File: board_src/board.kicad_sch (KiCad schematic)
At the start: 14 parts, among them J1 Conn_01x05, J16 Conn_01x05, J17 Conn_01x05, J18 Conn_02x20_Counter_Clockwise, J20 Conn_02x20_Counter_Clockwise, J21 Conn_02x20_Counter_Clockwise, J22 Conn_02x20_Counter_Clockwise, J6 Conn_01x03, J7 Conn_01x02, J8 Conn_01x03, SW1 SW_Push, SW2 SW_Push, U1 Pico, U4 Pico

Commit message: wersja 3d
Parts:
- removed J7: Conn_01x02, Connector_PinHeader_2.54mm:PinHeader_1x02_P2.54mm_Vertical, symbol Connector_Generic:Conn_01x02
- removed SW1, SW2: SW_Push, Button_Switch_THT:SW_PUSH_6mm, symbol Switch:SW_Push
- added J7: Conn_01x16, Connector_PinSocket_2.54mm:PinSocket_1x16_P2.54mm_Vertical, symbol Connector:Conn_01x16_Socket
- added S1, S2: 1301.9319, footprints:przycisk, symbol przycisk:1301.9319
- J18, J20, J21, J22: symbol Connector_Generic:Conn_02x20_Counter_Clockwise -> Connector_Generic:Conn_02x20_Odd_Even
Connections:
- net GND: now also S1.1 (NO_1), S2.1 (NO_1)
- net a1: now also J18.2 (Pin_2); no longer J18.40 (Pin_40)
- net a10: now also J18.19 (Pin_19), J18.20 (Pin_20); no longer J18.10 (Pin_10), J18.31 (Pin_31)
- net a11: now also J18.21 (Pin_21), J18.22 (Pin_22); no longer J18.11 (Pin_11), J18.30 (Pin_30)
- net a12: now also J18.23 (Pin_23), J18.24 (Pin_24); no longer J18.12 (Pin_12), J18.29 (Pin_29)
- net a13: now also J18.25 (Pin_25), J18.26 (Pin_26); no longer J18.13 (Pin_13), J18.28 (Pin_28)
- net a14: now also J18.28 (Pin_28); no longer J18.14 (Pin_14)
- net a15: now also J18.29 (Pin_29), J18.30 (Pin_30); no longer J18.15 (Pin_15), J18.26 (Pin_26)
- net a16: now also J18.31 (Pin_31), J18.32 (Pin_32); no longer J18.16 (Pin_16), J18.25 (Pin_25)
- net a17: now also J18.33 (Pin_33), J18.34 (Pin_34); no longer J18.17 (Pin_17), J18.24 (Pin_24)
- net a18: now also J18.35 (Pin_35), J18.36 (Pin_36); no longer J18.18 (Pin_18), J18.23 (Pin_23)
- net a19: now also J18.37 (Pin_37), J18.38 (Pin_38); no longer J18.19 (Pin_19), J18.22 (Pin_22)
- net a2: now also J18.3 (Pin_3), J18.4 (Pin_4); no longer J18.2 (Pin_2), J18.39 (Pin_39)
- net a20: now also J18.39 (Pin_39), J18.40 (Pin_40); no longer J18.20 (Pin_20), J18.21 (Pin_21)
- net a3: now also J18.5 (Pin_5), J18.6 (Pin_6); no longer J18.3 (Pin_3), J18.38 (Pin_38)
- net a4: now also J18.7 (Pin_7), J18.8 (Pin_8); no longer J18.37 (Pin_37), J18.4 (Pin_4)
- net a5: now also J18.10 (Pin_10), J18.9 (Pin_9); no longer J18.36 (Pin_36), J18.5 (Pin_5)
- net a6: now also J18.11 (Pin_11), J18.12 (Pin_12); no longer J18.35 (Pin_35), J18.6 (Pin_6)
- net a7: now also J18.13 (Pin_13), J18.14 (Pin_14); no longer J18.34 (Pin_34), J18.7 (Pin_7)
- net a8: now also J18.15 (Pin_15), J18.16 (Pin_16); no longer J18.33 (Pin_33), J18.8 (Pin_8)
- net a9: now also J18.17 (Pin_17), J18.18 (Pin_18); no longer J18.32 (Pin_32), J18.9 (Pin_9)
- net b1: now also J20.2 (Pin_2); no longer J20.40 (Pin_40)
- net b10: now also J20.19 (Pin_19), J20.20 (Pin_20); no longer J20.10 (Pin_10), J20.31 (Pin_31)
- net b11: now also J20.21 (Pin_21), J20.22 (Pin_22), S1.3 (COM_1); no longer J20.11 (Pin_11), J20.30 (Pin_30)
- net b12: now also J20.23 (Pin_23), J20.24 (Pin_24); no longer J20.12 (Pin_12), J20.29 (Pin_29)
- net b13: now also J20.25 (Pin_25), J20.26 (Pin_26); no longer J20.13 (Pin_13), J20.28 (Pin_28)
- net b14: now also J20.28 (Pin_28); no longer J20.14 (Pin_14)
- net b15: now also J20.29 (Pin_29), J20.30 (Pin_30); no longer J20.15 (Pin_15), J20.26 (Pin_26)
- net b16: now also J20.31 (Pin_31), J20.32 (Pin_32); no longer J20.16 (Pin_16), J20.25 (Pin_25)
- net b17: now also J20.33 (Pin_33), J20.34 (Pin_34); no longer J20.17 (Pin_17), J20.24 (Pin_24)
- net b18: now also J20.35 (Pin_35), J20.36 (Pin_36); no longer J20.18 (Pin_18), J20.23 (Pin_23)
- net b19: now also J20.37 (Pin_37), J20.38 (Pin_38); no longer J20.19 (Pin_19), J20.22 (Pin_22)
- net b2: now also J20.3 (Pin_3), J20.4 (Pin_4); no longer J20.2 (Pin_2), J20.39 (Pin_39)
- net b20: now also J20.39 (Pin_39), J20.40 (Pin_40); no longer J20.20 (Pin_20), J20.21 (Pin_21)
- net b3: now also J20.5 (Pin_5), J20.6 (Pin_6); no longer J20.3 (Pin_3), J20.38 (Pin_38)
- net b4: now also J20.7 (Pin_7), J20.8 (Pin_8); no longer J20.37 (Pin_37), J20.4 (Pin_4)
- net b5: now also J20.10 (Pin_10), J20.9 (Pin_9); no longer J20.36 (Pin_36), J20.5 (Pin_5)
- net b6: now also J20.11 (Pin_11), J20.12 (Pin_12); no longer J20.35 (Pin_35), J20.6 (Pin_6)
- net b7: now also J20.13 (Pin_13), J20.14 (Pin_14); no longer J20.34 (Pin_34), J20.7 (Pin_7)
- net b8: now also J20.15 (Pin_15), J20.16 (Pin_16); no longer J20.33 (Pin_33), J20.8 (Pin_8)
- net b9: now also J20.17 (Pin_17), J20.18 (Pin_18); no longer J20.32 (Pin_32), J20.9 (Pin_9)
- net c1: now also J21.2 (Pin_2); no longer J21.40 (Pin_40)
- net c10: now also J21.19 (Pin_19), J21.20 (Pin_20); no longer J21.10 (Pin_10), J21.31 (Pin_31)
- net c11: now also J21.21 (Pin_21), J21.22 (Pin_22); no longer J21.11 (Pin_11), J21.30 (Pin_30)
- net c12: now also J21.23 (Pin_23), J21.24 (Pin_24); no longer J21.12 (Pin_12), J21.29 (Pin_29)
- net c13: now also J21.25 (Pin_25), J21.26 (Pin_26); no longer J21.13 (Pin_13), J21.28 (Pin_28)
- net c14: now also J21.28 (Pin_28); no longer J21.14 (Pin_14)
- net c15: now also J21.29 (Pin_29), J21.30 (Pin_30); no longer J21.15 (Pin_15), J21.26 (Pin_26)
- net c16: now also J21.31 (Pin_31), J21.32 (Pin_32); no longer J21.16 (Pin_16), J21.25 (Pin_25)
- net c17: now also J21.33 (Pin_33), J21.34 (Pin_34); no longer J21.17 (Pin_17), J21.24 (Pin_24)
- net c18: now also J21.35 (Pin_35), J21.36 (Pin_36); no longer J21.18 (Pin_18), J21.23 (Pin_23)
- net c19: now also J21.37 (Pin_37), J21.38 (Pin_38); no longer J21.19 (Pin_19), J21.22 (Pin_22)
- net c2: now also J21.3 (Pin_3), J21.4 (Pin_4); no longer J21.2 (Pin_2), J21.39 (Pin_39)
- net c20: now also J21.39 (Pin_39), J21.40 (Pin_40); no longer J21.20 (Pin_20), J21.21 (Pin_21)
- net c3: now also J21.5 (Pin_5), J21.6 (Pin_6); no longer J21.3 (Pin_3), J21.38 (Pin_38)
- net c4: now also J21.7 (Pin_7), J21.8 (Pin_8); no longer J21.37 (Pin_37), J21.4 (Pin_4)
- net c5: now also J21.10 (Pin_10), J21.9 (Pin_9); no longer J21.36 (Pin_36), J21.5 (Pin_5)
- net c6: now also J21.11 (Pin_11), J21.12 (Pin_12); no longer J21.35 (Pin_35), J21.6 (Pin_6)
- net c7: now also J21.13 (Pin_13), J21.14 (Pin_14); no longer J21.34 (Pin_34), J21.7 (Pin_7)
- net c8: now also J21.15 (Pin_15), J21.16 (Pin_16); no longer J21.33 (Pin_33), J21.8 (Pin_8)
- net c9: now also J21.17 (Pin_17), J21.18 (Pin_18); no longer J21.32 (Pin_32), J21.9 (Pin_9)
- net d1: now also J22.2 (Pin_2); no longer J22.40 (Pin_40)
- net d10: now also J22.19 (Pin_19), J22.20 (Pin_20); no longer J22.10 (Pin_10), J22.31 (Pin_31)
- net d11: now also J22.21 (Pin_21), J22.22 (Pin_22), S2.3 (COM_1); no longer J22.11 (Pin_11), J22.30 (Pin_30)
- net d12: now also J22.23 (Pin_23), J22.24 (Pin_24); no longer J22.12 (Pin_12), J22.29 (Pin_29)
- net d13: now also J22.25 (Pin_25), J22.26 (Pin_26); no longer J22.13 (Pin_13), J22.28 (Pin_28)
- net d14: now also J22.28 (Pin_28); no longer J22.14 (Pin_14)
- net d15: now also J22.29 (Pin_29), J22.30 (Pin_30); no longer J22.15 (Pin_15), J22.26 (Pin_26)
- net d16: now also J22.31 (Pin_31), J22.32 (Pin_32); no longer J22.16 (Pin_16), J22.25 (Pin_25)
- net d17: now also J22.33 (Pin_33), J22.34 (Pin_34); no longer J22.17 (Pin_17), J22.24 (Pin_24)
- net d18: now also J22.35 (Pin_35), J22.36 (Pin_36); no longer J22.18 (Pin_18), J22.23 (Pin_23)
- net d19: now also J22.37 (Pin_37), J22.38 (Pin_38); no longer J22.19 (Pin_19), J22.22 (Pin_22)
- net d2: now also J22.3 (Pin_3), J22.4 (Pin_4); no longer J22.2 (Pin_2), J22.39 (Pin_39)
- net d20: now also J22.39 (Pin_39), J22.40 (Pin_40); no longer J22.20 (Pin_20), J22.21 (Pin_21)
- net d3: now also J22.5 (Pin_5), J22.6 (Pin_6); no longer J22.3 (Pin_3), J22.38 (Pin_38)
- net d4: now also J22.7 (Pin_7), J22.8 (Pin_8); no longer J22.37 (Pin_37), J22.4 (Pin_4)
- net d5: now also J22.10 (Pin_10), J22.9 (Pin_9); no longer J22.36 (Pin_36), J22.5 (Pin_5)
- net d6: now also J22.11 (Pin_11), J22.12 (Pin_12); no longer J22.35 (Pin_35), J22.6 (Pin_6)
- net d7: now also J22.13 (Pin_13), J22.14 (Pin_14); no longer J22.34 (Pin_34), J22.7 (Pin_7)
- net d8: now also J22.15 (Pin_15), J22.16 (Pin_16); no longer J22.33 (Pin_33), J22.8 (Pin_8)
- net d9: now also J22.17 (Pin_17), J22.18 (Pin_18); no longer J22.32 (Pin_32), J22.9 (Pin_9)
- no-connect marks 0 -> 4
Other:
- note added: "Czy robimy Raspberry na stałe czy nóżki?"
- note added: "przetwornik cyfra-analog"
- note added: "wyprowadzenia wyświetlacza"
- moved on the sheet: J1, J16, J17, J20, J22, J6, J8

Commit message: uporzadkowane 3D
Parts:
- added J26: Conn_01x16, Connector_PinHeader_2.54mm:PinHeader_1x16_P2.54mm_Vertical, symbol Connector_Generic:Conn_01x16
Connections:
- net at J7.1 (Pin_1): now also J26.16 (Pin_16)
- net at J7.10 (Pin_10): now also J26.7 (Pin_7)
- net at J7.11 (Pin_11): now also J26.6 (Pin_6)
- net at J7.12 (Pin_12): now also J26.5 (Pin_5)
- net at J7.13 (Pin_13): now also J26.4 (Pin_4)
- net at J7.14 (Pin_14): now also J26.3 (Pin_3)
- net at J7.15 (Pin_15): now also J26.2 (Pin_2)
- net at J7.16 (Pin_16): now also J26.1 (Pin_1)
- net at J7.2 (Pin_2): now also J26.15 (Pin_15)
- net at J7.3 (Pin_3): now also J26.14 (Pin_14)
- net at J7.4 (Pin_4): now also J26.13 (Pin_13)
- net at J7.5 (Pin_5): now also J26.12 (Pin_12)
- net at J7.6 (Pin_6): now also J26.11 (Pin_11)
- net at J7.7 (Pin_7): now also J26.10 (Pin_10)
- net at J7.8 (Pin_8): now also J26.9 (Pin_9)
- net at J7.9 (Pin_9): now also J26.8 (Pin_8)
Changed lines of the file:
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@@
 	(wire
 		(pts
+			(xy 222.25 101.6) (xy 228.6 101.6)
+		)
+		(stroke
+			(width 0)
+			(type default)
+		)
+	)
+	(wire
+		(pts
 			(xy 45.72 33.02) (xy 50.8 33.02)
 		)
@@
 	(wire
 		(pts
+			(xy 222.25 109.22) (xy 228.6 109.22)
+		)
+		(stroke
+			(width 0)
+			(type default)
+		)
+	)
+	(wire
+		(pts
 			(xy 142.24 38.1) (xy 142.24 39.37)
 		)
@@
 	(wire
 		(pts
+			(xy 222.25 129.54) (xy 228.6 129.54)
+		)
+		(stroke
+			(width 0)
+			(type default)
+		)
+	)
+	(wire
+		(pts
 			(xy 213.36 74.93) (xy 213.36 73.66)
 		)
@@
 	(wire
 		(pts
+			(xy 222.25 106.68) (xy 228.6 106.68)
+		)
+		(stroke
+			(width 0)
+			(type default)
+		)
+	)
+	(wire
+		(pts
 			(xy 45.72 68.58) (xy 50.8 68.58)
 		)
@@
 	(wire
 		(pts
+			(xy 222.25 93.98) (xy 228.6 93.98)
+		)
+		(stroke
+			(width 0)
+			(type default)
+		)
+	)
+	(wire
+		(pts
 			(xy 182.88 27.94) (xy 185.42 27.94)
 		)
@@
 	(wire
 		(pts
+			(xy 222.25 96.52) (xy 228.6 96.52)
+		)
+		(stroke
+			(width 0)
+			(type default)
+		)
+	)
+	(wire
+		(pts
 			(xy 255.27 60.96) (xy 259.08 60.96)
 		)
@@
 	(wire
 		(pts
+			(xy 222.25 104.14) (xy 228.6 104.14)
+		)
+		(stroke
+			(width 0)
+			(type default)
+		)
+	)
+	(wire
+		(pts
 			(xy 255.27 55.88) (xy 259.08 55.88)
 		)
@@
 	(wire
 		(pts
+			(xy 222.25 124.46) (xy 228.6 124.46)
+		)
+		(stroke
+			(width 0)
+			(type default)
+		)
+	)
+	(wire
+		(pts
 			(xy 137.16 68.58) (xy 139.7 68.58)
 		)
@@
 	(wire
 		(pts
+			(xy 222.25 127) (xy 228.6 127)
+		)
+		(stroke
+			(width 0)
+			(type default)
+		)
+	)
+	(wire
+		(pts
 			(xy 45.72 53.34) (xy 50.8 53.34)
 		)
@@
 	(wire
 		(pts
+			(xy 222.25 111.76) (xy 228.6 111.76)
+		)
+		(stroke
+			(width 0)
+			(type default)
+		)
+	)
+	(wire
+		(pts
 			(xy 213.36 76.2) (xy 213.36 74.93)
 		)
@@
 	(wire
 		(pts
+			(xy 222.25 91.44) (xy 228.6 91.44)
+		)
+		(stroke
+			(width 0)
+			(type default)
+		)
+	)
+	(wire
+		(pts
 			(xy 68.58 77.47) (xy 68.58 74.93)
 		)
@@
 	(wire
 		(pts
+			(xy 222.25 116.84) (xy 228.6 116.84)
+		)
+		(stroke
+			(width 0)
+			(type default)
+		)
+	)
+	(wire
+		(pts
 			(xy 97.79 78.74) (xy 102.87 78.74)
 		)
@@
 	(wire
 		(pts
+			(xy 222.25 119.38) (xy 228.6 119.38)
+		)
+		(stroke
+			(width 0)
+			(type default)
+		)
+	)
+	(wire
+		(pts
 			(xy 182.88 40.64) (xy 185.42 40.64)
 		)
@@
 	(wire
 		(pts
+			(xy 222.25 114.3) (xy 228.6 114.3)
+		)
+		(stroke
+			(width 0)
+			(type default)
+		)
+	)
+	(wire
+		(pts
 			(xy 166.37 33.02) (xy 170.18 33.02)
 		)
@@
 	(wire
 		(pts
+			(xy 222.25 121.92) (xy 228.6 121.92)
+		)
+		(stroke
+			(width 0)
+			(type default)
+		)
+	)
+	(wire
+		(pts
 			(xy 71.12 73.66) (xy 71.12 74.93)
 		)
@@
 	(wire
 		(pts
+			(xy 222.25 99.06) (xy 228.6 99.06)
+		)
+		(stroke
+			(width 0)
+			(type default)
+		)
+	)
+	(wire
+		(pts
 			(xy 137.16 54.61) (xy 139.7 54.61)
 		)
@@
 					(unit 1)
 				)
+			)
+		)
+	)
+	(symbol
+		(lib_id "Connector_Generic:Conn_01x16")
+		(at 217.17 111.76 180)
+		(unit 1)
+		(exclude_from_sim no)
+		(in_bom yes)
+		(on_board yes)
+		(dnp no)
+		(fields_autoplaced yes)
+		(property "Reference" "J26"
+			(at 217.17 85.09 0)
+			(effects
+				(font
+					(size 1.27 1.27)
+				)
+			)
+		)
+		(property "Value" "Conn_01x16"
+			(at 217.17 87.63 0)
+			(effects
+				(font
+					(size 1.27 1.27)
+				)
+			)
+		)
+		(property "Footprint" "Connector_PinHeader_2.54mm:PinHeader_1x16_P2.54mm_Vertical"
+			(at 217.17 111.76 0)
+			(effects
+				(font
+					(size 1.27 1.27)
+				)
+				(hide yes)
+			)
+		)
+		(property "Datasheet" "~"
+			(at 217.17 111.76 0)
+			(effects
+				(font
+					(size 1.27 1.27)
+				)
+				(hide yes)
+			)
+		)
+		(property "Description" "Generic connector, single row, 01x16, script generated (kicad-library-utils/schlib/autogen/connector/)"
+			(at 217.17 111.76 0)
+			(effects
+				(font
+					(size 1.27 1.27)
+				)
+				(hide yes)
+			)
+		)
+		(pin "3"
+		)
+		(pin "6"
+		)
+		(pin "12"
+		)
+		(pin "15"
+		)
+		(pin "4"
+		)
+		(pin "9"
+		)
+		(pin "10"
+		)
+		(pin "11"
+		)
+		(pin "7"
+		)
+		(pin "14"
+		)
+		(pin "1"
+		)
+		(pin "2"
+		)
+		(pin "5"
+		)
+		(pin "8"
+		)
+		(pin "13"
+		)
+		(pin "16"
+		)
+		(instances
+			(project ""
+				(path "/772e9f49-cfcf-4cf6-843d-0684684f2d4b"
+					(reference "J26")
+					(unit 1)
+				)

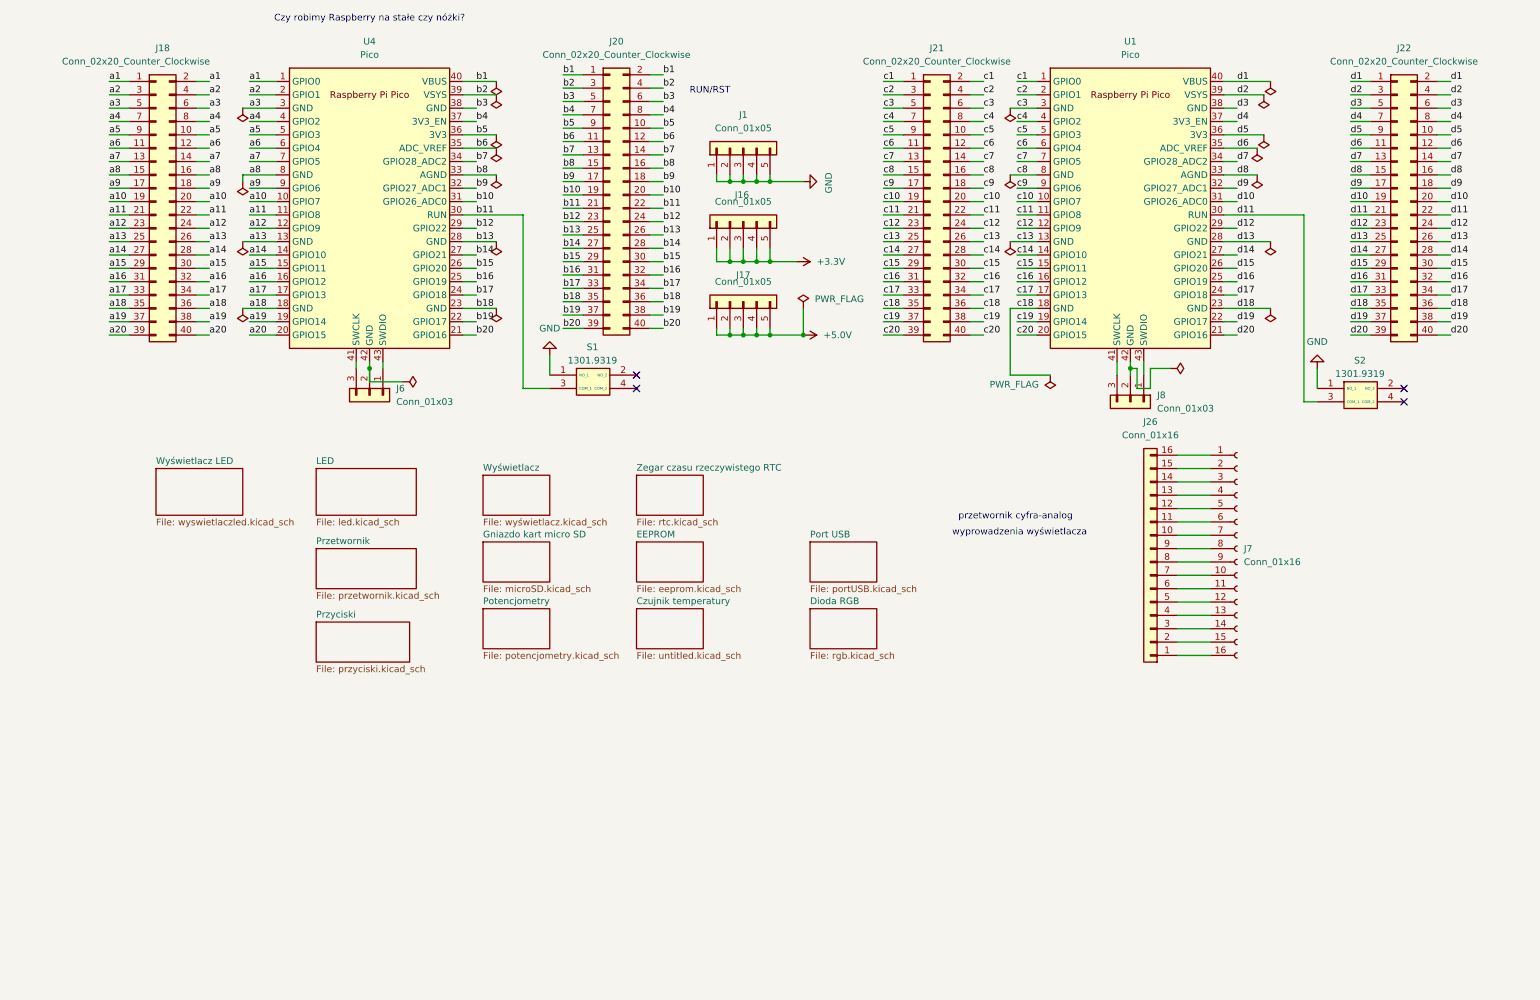
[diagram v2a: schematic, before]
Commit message: wersja z wyswietlaczem LCD
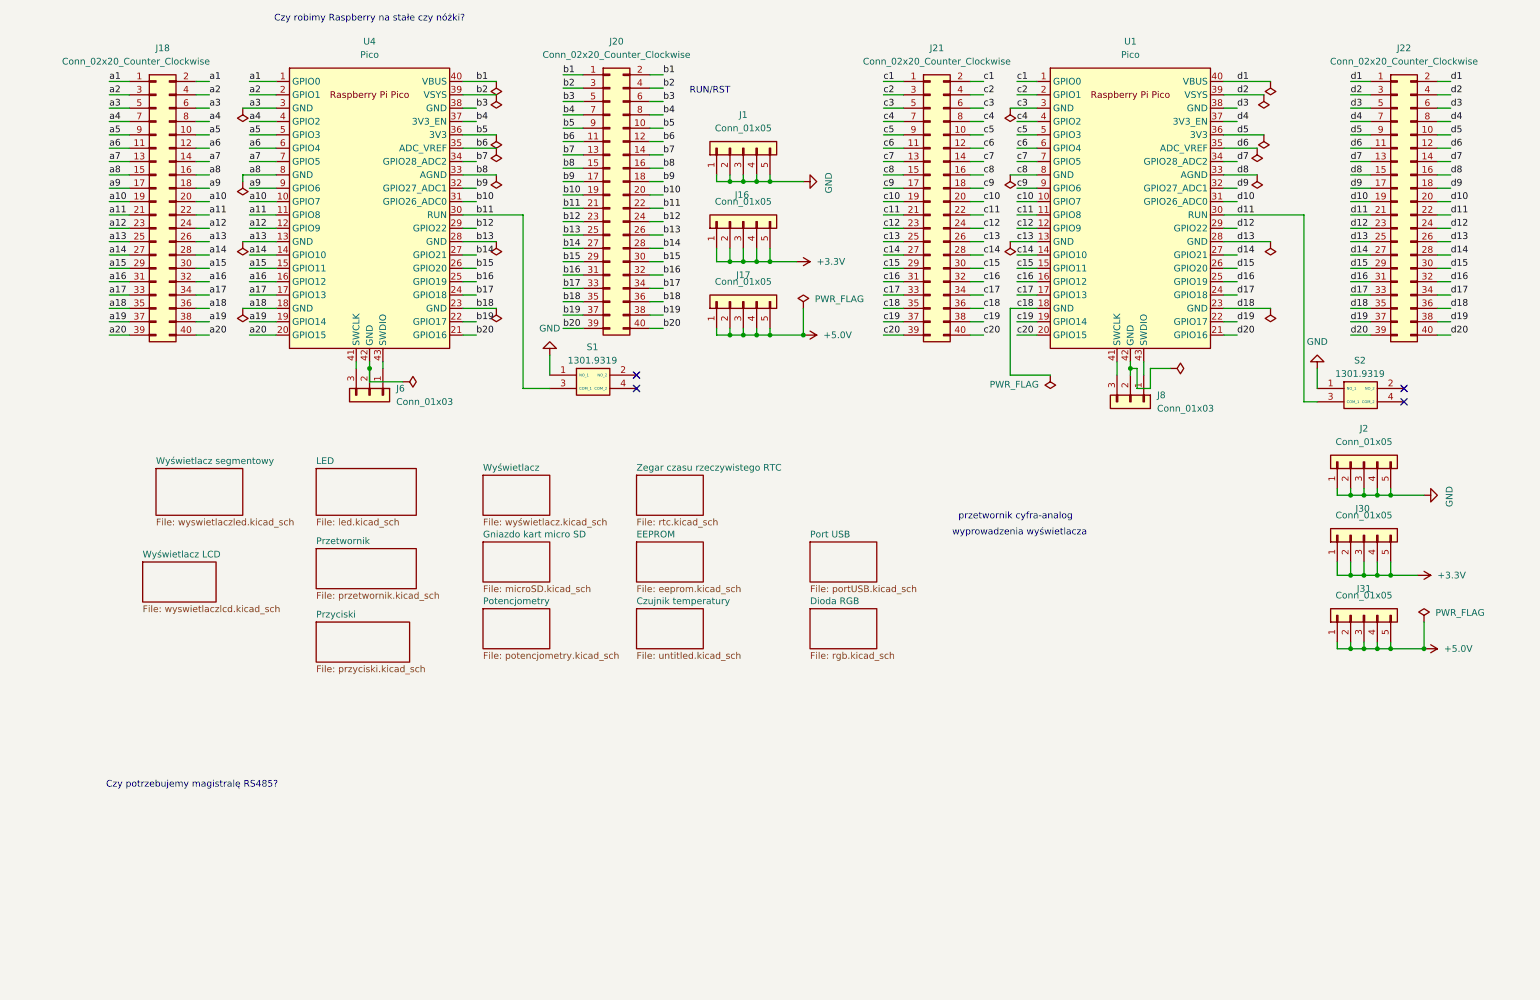
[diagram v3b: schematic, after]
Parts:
- removed J26: Conn_01x16, Connector_PinHeader_2.54mm:PinHeader_1x16_P2.54mm_Vertical, symbol Connector_Generic:Conn_01x16
- removed J7: Conn_01x16, Connector_PinSocket_2.54mm:PinSocket_1x16_P2.54mm_Vertical, symbol Connector:Conn_01x16_Socket
- added J2, J30, J31: Conn_01x05, Connector_PinHeader_2.54mm:PinHeader_1x05_P2.54mm_Vertical, symbol Connector_Generic:Conn_01x05
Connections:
- net +3.3V: now also J30.1 (Pin_1), J30.2 (Pin_2), J30.3 (Pin_3), J30.4 (Pin_4), J30.5 (Pin_5)
- net +5.0V: now also J31.1 (Pin_1), J31.2 (Pin_2), J31.3 (Pin_3), J31.4 (Pin_4), J31.5 (Pin_5)
- net GND: now also J2.1 (Pin_1), J2.2 (Pin_2), J2.3 (Pin_3), J2.4 (Pin_4), J2.5 (Pin_5)
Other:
- sheet Wyświetlacz LED renamed Wyświetlacz segmentowy
- added sheet Wyświetlacz LCD (wyswietlaczlcd.kicad_sch)
- note added: "Czy potrzebujemy magistralę RS485?"

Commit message: wersja z FT232RN
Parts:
- removed J6, J8: Conn_01x03, Connector_PinHeader_2.54mm:PinHeader_1x03_P2.54mm_Vertical, symbol Connector_Generic:Conn_01x03
- added J26, J28: Conn_01x20_Socket, symbol Connector:Conn_01x20_Socket
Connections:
- net b1 renamed VBUS
- net b2 renamed VSYS
- new net: J26.1 (Pin_1), J26.10 (Pin_10), J26.11 (Pin_11), J26.12 (Pin_12), J26.13 (Pin_13), J26.14 (Pin_14), J26.15 (Pin_15), J26.16 (Pin_16), J26.17 (Pin_17), J26.18 (Pin_18), J26.19 (Pin_19), J26.2 (Pin_2), J26.20 (Pin_20), J26.3 (Pin_3), J26.4 (Pin_4), J26.5 (Pin_5), J26.6 (Pin_6), J26.7 (Pin_7), J26.8 (Pin_8), J26.9 (Pin_9)
- new net: J28.1 (Pin_1), J28.10 (Pin_10), J28.11 (Pin_11), J28.12 (Pin_12), J28.13 (Pin_13), J28.14 (Pin_14), J28.15 (Pin_15), J28.16 (Pin_16), J28.17 (Pin_17), J28.18 (Pin_18), J28.19 (Pin_19), J28.2 (Pin_2), J28.20 (Pin_20), J28.3 (Pin_3), J28.4 (Pin_4), J28.5 (Pin_5), J28.6 (Pin_6), J28.7 (Pin_7), J28.8 (Pin_8), J28.9 (Pin_9)
- no-connect marks 4 -> 13
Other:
- sheet Przetwornik renamed Przetwornik analoowo-cyfrowy
- note added: "FTDI FT232RL"
- moved on the sheet: J18
